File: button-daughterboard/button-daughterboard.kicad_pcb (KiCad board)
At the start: 2 copper layers, 26 x 26 mm, 16 parts, among them J1 Conn_01x01, J2 Conn_01x01, J3 Conn_01x01, J4 Conn_01x01, J5 Conn_01x01, SW1 SW_Push, SW2 SW_Push, SW3 SW_Push, SW4 SW_Push

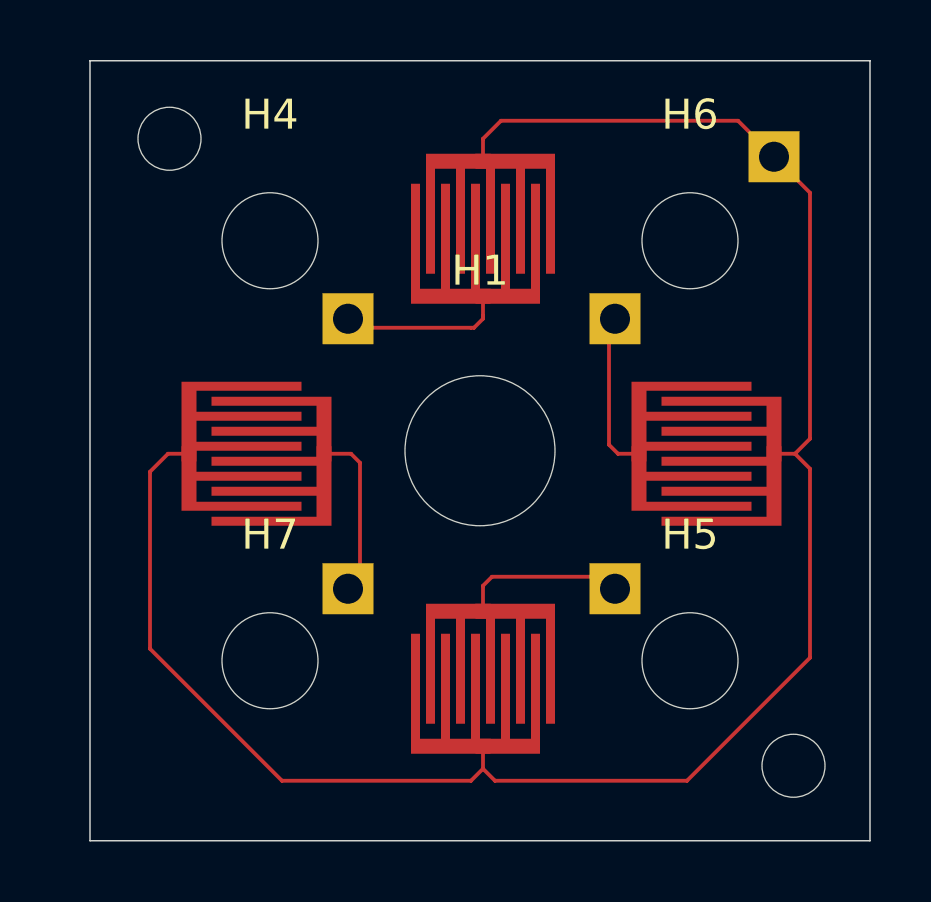
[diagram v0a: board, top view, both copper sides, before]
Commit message: Add D-Pad 3d model
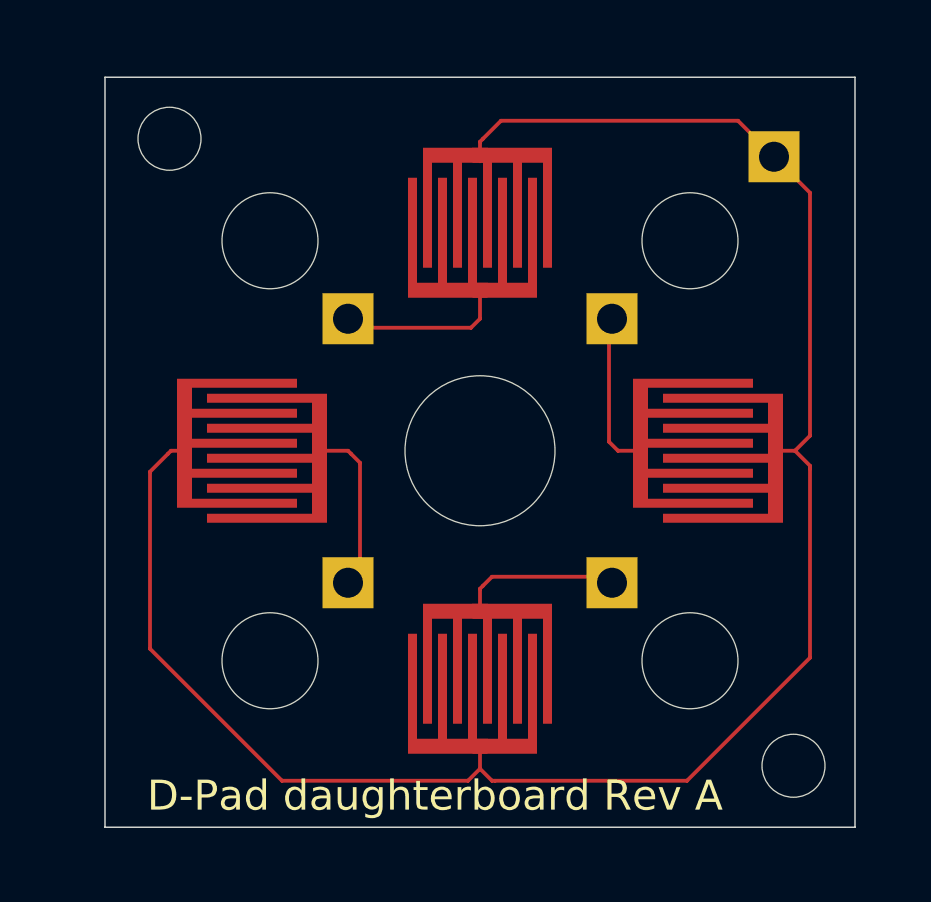
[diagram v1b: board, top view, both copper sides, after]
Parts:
- moved J3 0.22 mm to (104.4, 104.4)
- moved SW4 0.22 mm to (100.0, 92.4)
- moved J2 0.20 mm to (95.6, 104.4)
- moved SW2 0.18 mm to (92.4, 100.0)
- moved SW1 0.11 mm to (107.6, 100.0)
- moved J1 0.10 mm to (104.4, 95.6)
- moved SW3 0.10 mm to (100.0, 107.6)
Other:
- board size 26 x 26 mm -> 25 x 25 mm
- board text added: "D-Pad daughterboard Rev A"

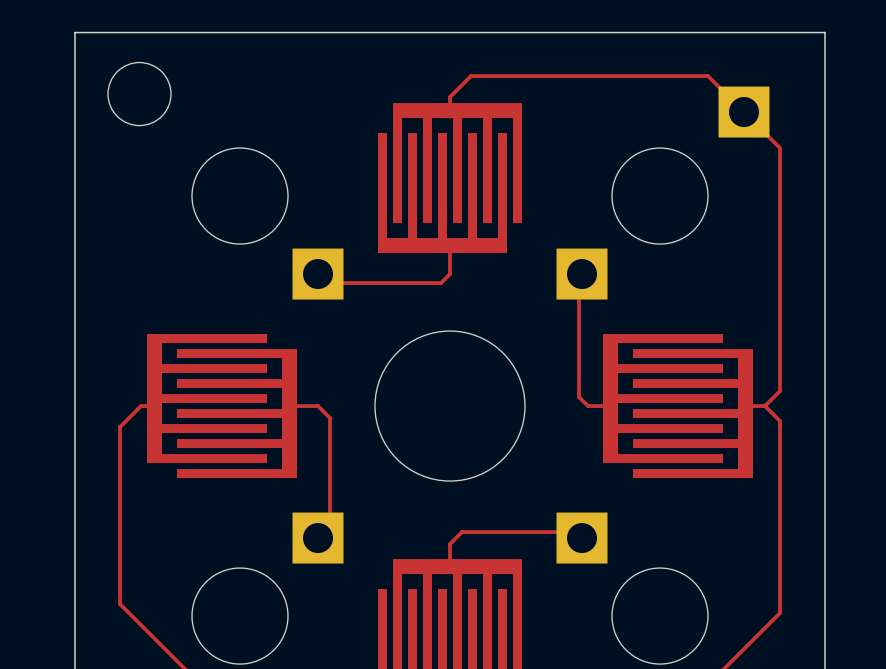
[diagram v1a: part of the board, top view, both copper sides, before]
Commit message: Add option for elevated D-Pad
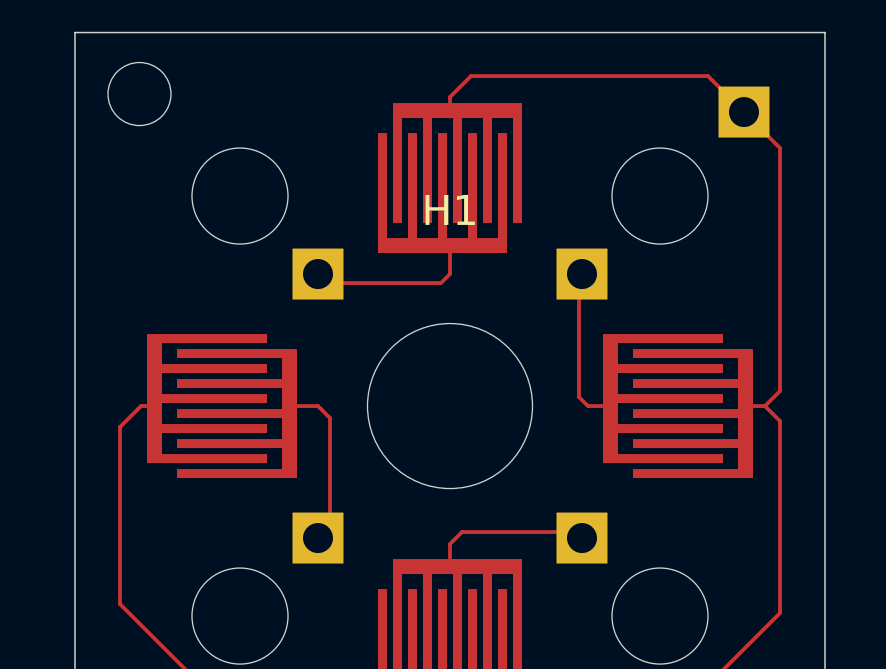
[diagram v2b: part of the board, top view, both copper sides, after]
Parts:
- H1: footprint MountingHole:MountingHole_5mm -> MountingHole:MountingHole_5.5mm
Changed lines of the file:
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@@
     (mod_text_size 1 1)
     (mod_text_width 0.15)
-    (pad_size 1.524 1.524)
-    (pad_drill 0.762)
+    (pad_size 5.5 5.5)
+    (pad_drill 5.5)
     (pad_to_mask_clearance 0)
     (aux_axis_origin 0 0)
@@
     (add_net "Net-(J4-Pad1)")
   )
+  (module MountingHole:MountingHole_5.5mm (layer F.Cu)
+    (at 100 100)
+    (descr "Mounting Hole 5.5mm, no annular")
+    (tags "mounting hole 5.5mm no annular")
+    (attr virtual)
+    (fp_text reference H1 (at 0 -6.5) (layer F.SilkS)
+      (effects (font (size 1 1) (thickness 0.15)))
+    )
+    (fp_text value "D-Pad Hole" (at 0 6.5) (layer F.Fab)
+      (effects (font (size 1 1) (thickness 0.15)))
+    )
+    (fp_text user %R (at 0.3 0) (layer F.Fab)
+      (effects (font (size 1 1) (thickness 0.15)))
+    )
+    (fp_circle (center 0 0) (end 5.5 0) (layer Cmts.User) (width 0.15))
+    (fp_circle (center 0 0) (end 5.75 0) (layer F.CrtYd) (width 0.05))
+    (pad 1 np_thru_hole circle (at 0 0) (size 5.5 5.5) (drill 5.5) (layers *.Cu *.Mask))
+  )
   (module Connector_PinHeader_2.54mm:PinHeader_1x01_P2.54mm_Vertical (layer B.Cu)
     (at 109.8 90.2)
@@
     (pad 1 np_thru_hole circle (at 0 0) (size 3.2 3.2) (drill 3.2) (layers *.Cu *.Mask))
   )
-  (module MountingHole:MountingHole_5mm (layer F.Cu)
-    (at 100 100)
-    (descr "Mounting Hole 5mm, no annular")
-    (tags "mounting hole 5mm no annular")
-    (attr virtual)
-    (fp_text reference H1 (at 0 -6) (layer F.SilkS) hide
-      (effects (font (size 1 1) (thickness 0.15)))
-    )
-    (fp_text value "D-Pad Hole" (at 0 6) (layer F.Fab)
-      (effects (font (size 1 1) (thickness 0.15)))
-    )
-    (fp_circle (center 0 0) (end 5.25 0) (layer F.CrtYd) (width 0.05))
-    (fp_circle (center 0 0) (end 5 0) (layer Cmts.User) (width 0.15))
-    (fp_text user %R (at 0.3 0) (layer F.Fab)
-      (effects (font (size 1 1) (thickness 0.15)))
-    )
-    (pad 1 np_thru_hole circle (at 0 0) (size 5 5) (drill 5) (layers *.Cu *.Mask))
-  )
   (module Button_Carbon:Button_Carbon_5mm (layer F.Cu)

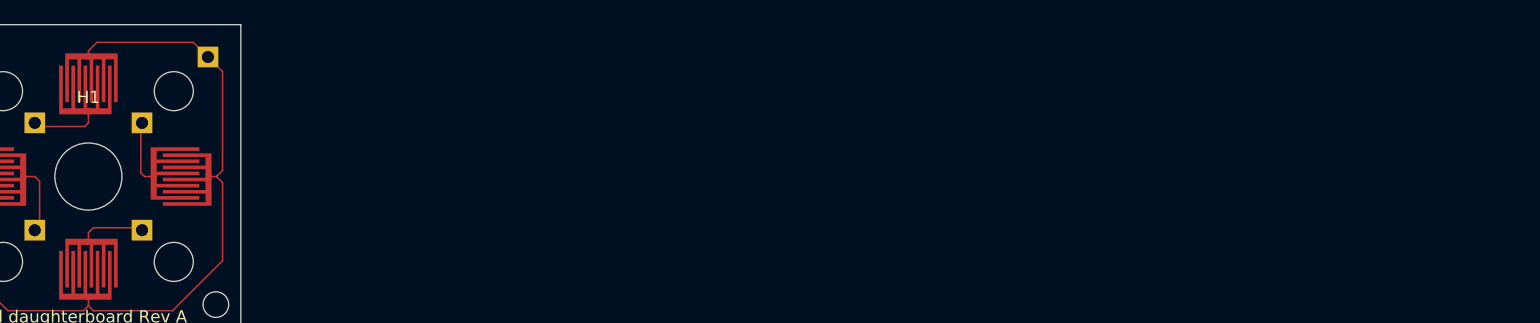
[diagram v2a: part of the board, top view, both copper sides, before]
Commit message: Add AB buttons
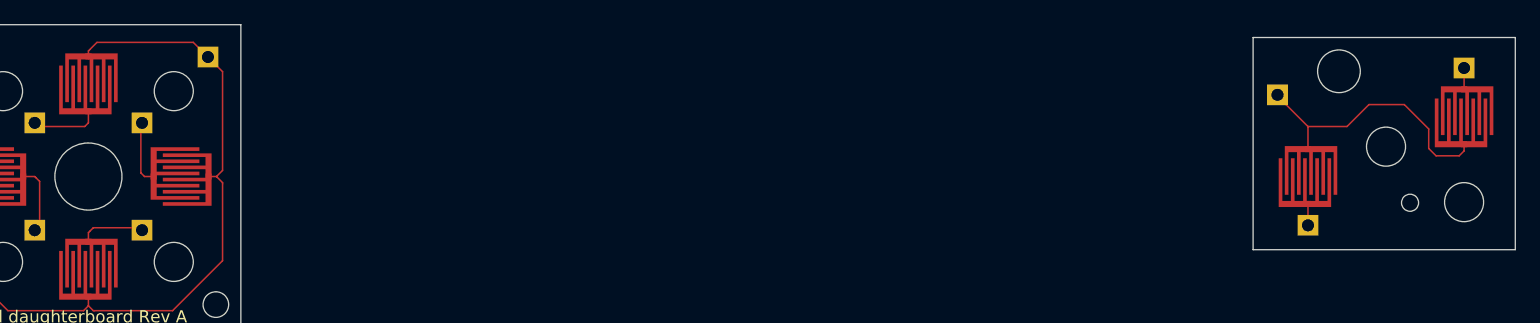
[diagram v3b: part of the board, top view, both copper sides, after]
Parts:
- added H10: MountingHole, MountingHole:MountingHole_3.2mm_M3, F.Cu at (206.4, 97.5)
- added H11: MountingHole, MountingHole:MountingHole_3.2mm_M3, F.Cu at (212.8, 102.1)
- added H8: AB top left, MountingHole:MountingHole_3.5mm, F.Cu at (202.5, 91.4)
- added H9: AB bottom right, MountingHole_GBA:MountingHole_GBA_AB_bottom_right, F.Cu at (208.4, 102.2)
- added J6: Conn_01x01, Connector_PinHeader_2.54mm:PinHeader_1x01_P2.54mm_Vertical, B.Cu at (200.0, 104.0)
- added J7: Conn_01x01, Connector_PinHeader_2.54mm:PinHeader_1x01_P2.54mm_Vertical, B.Cu at (197.5, 93.3)
- added J8: Conn_01x01, Connector_PinHeader_2.54mm:PinHeader_1x01_P2.54mm_Vertical, B.Cu at (212.8, 91.1)
- added SW5: SW_Push, Button_Carbon:Button_Carbon_5mm, F.Cu at (200.0, 100.0)
- added SW6: SW_Push, Button_Carbon:Button_Carbon_5mm, F.Cu at (212.8, 95.1)
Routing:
- net GND: track 63.6 -> 85.9 mm
- net Net-(J6-Pad1): track 0.00 -> 1.80 mm
- net Net-(J8-Pad1): track 0.00 -> 1.70 mm
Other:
- board size 25 x 25 mm -> 129.5 x 25 mm

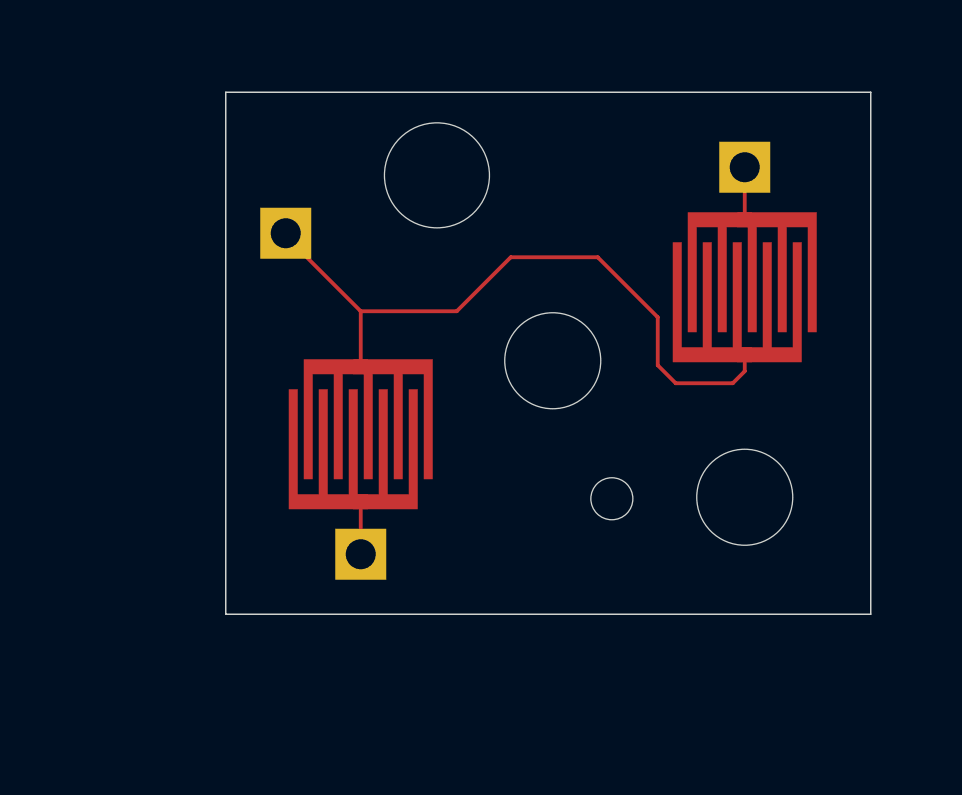
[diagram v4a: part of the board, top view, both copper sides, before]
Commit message: Add some margin left of B button
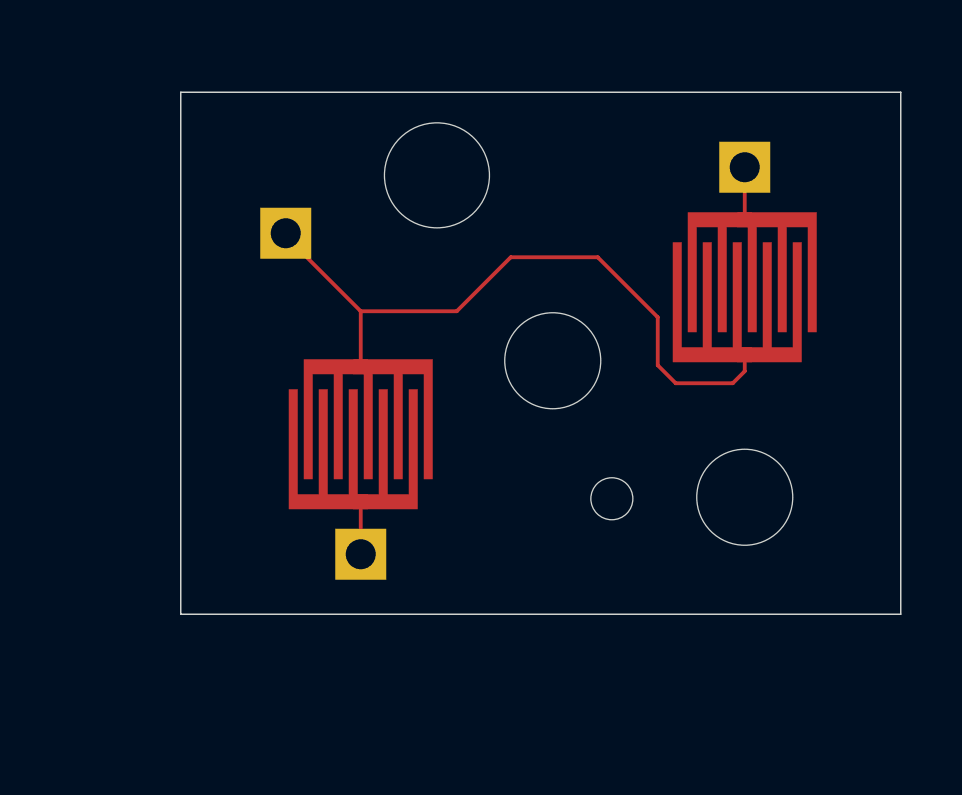
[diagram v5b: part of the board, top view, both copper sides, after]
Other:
- board size 129.5 x 25 mm -> 130.5 x 25 mm
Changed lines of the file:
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@@
     (effects (font (size 1 1) (thickness 0.15)))
   )
-  (gr_line (start 195.5 88.6) (end 195.5 106) (layer Edge.Cuts) (width 0.05))
-  (gr_line (start 217 106) (end 195.5 106) (layer Edge.Cuts) (width 0.05))
-  (gr_line (start 217 88.6) (end 217 106) (layer Edge.Cuts) (width 0.05))
-  (gr_line (start 195.5 88.6) (end 217 88.6) (layer Edge.Cuts) (width 0.05))
+  (gr_line (start 194 88.6) (end 194 106) (layer Edge.Cuts) (width 0.05))
+  (gr_line (start 218 106) (end 194 106) (layer Edge.Cuts) (width 0.05))
+  (gr_line (start 218 88.6) (end 218 106) (layer Edge.Cuts) (width 0.05))
+  (gr_line (start 194 88.6) (end 218 88.6) (layer Edge.Cuts) (width 0.05))
   (segment (start 104.6 100) (end 104.3 99.7) (width 0.127) (layer F.Cu) (net 1))
   (segment (start 104.3 99.7) (end 104.3 95.9) (width 0.127) (layer F.Cu) (net 1))
